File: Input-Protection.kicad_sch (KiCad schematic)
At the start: 0 parts

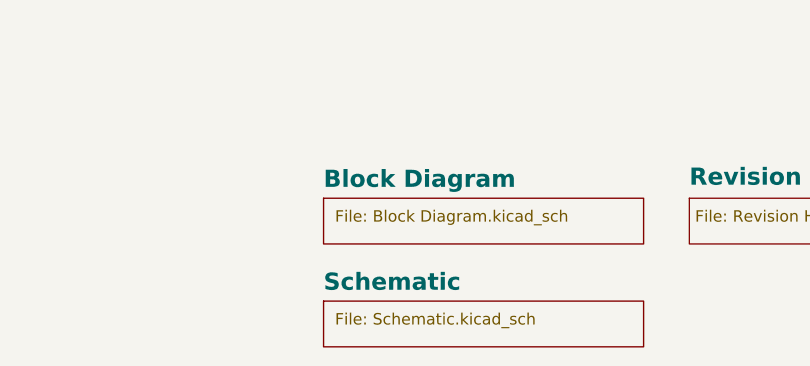
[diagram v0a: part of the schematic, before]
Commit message: fix: fix properties of actives with MPN
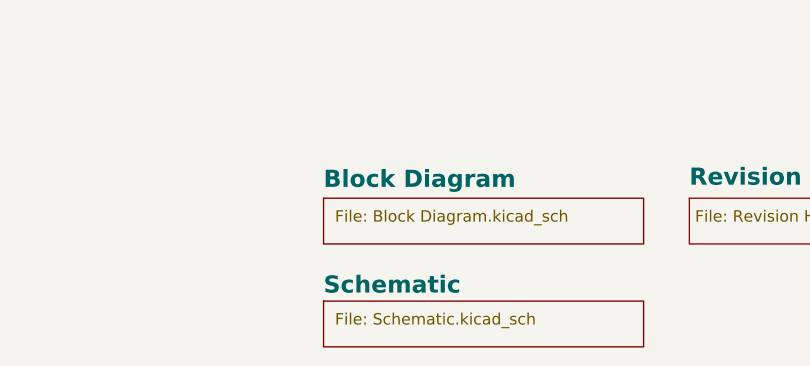
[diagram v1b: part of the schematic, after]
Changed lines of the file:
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@@
 		)
 		(property "Sheetname" "Schematic"
-			(at 299.72 312.6609 0)
+			(at 299.72 312.9784 0)
 			(effects
 				(font

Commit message: fix: template changes
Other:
- note added: "CHECKED - There shouldn't be any mistakes. Contact the engineer if found."
- note removed: "CHECKED - There shouldn't be any mistakes. Contact the engineer if you find any."
- note removed: "Date: ${RELEASE_DATE}"

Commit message: feat: preliminary pcb layout
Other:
- sheet Revision History renamed REVISION HISTORY
- removed sheet Block Diagram
- removed sheet Schematic
- added sheet ARCHITECTURE (Project Architecture.kicad_sch)
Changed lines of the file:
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@@
 	(text "TOP VIEW"
 		(exclude_from_sim no)
-		(at 22.86 166.37 0)
+		(at 27.94 166.37 0)
 		(effects
 			(font
@@
 		(effects
 			(font
-				(face "Arial")
 				(size 5 5)
 				(bold yes)
@@
 	(text_box "kibot_image_png_3d_viewer_angled_top"
 		(exclude_from_sim no)
-		(at 22.86 166.37 0)
+		(at 27.94 166.37 0)
 		(size 69.85 78.74)
 		(margins 1.905 1.905 1.905 1.905)
@@
 			(type dot)
 			(color 0 0 0 1)
+		)
+	)
+	(sheet
+		(at 299.72 313.69)
+		(size 35.56 5.08)
+		(exclude_from_sim no)
+		(in_bom yes)
+		(on_board yes)
+		(dnp no)
+		(stroke
+			(width 0.1524)
+			(type solid)
+		)
+		(fill
+			(color 0 0 0 0.0000)
+		)
+		(property "Sheetname" "ARCHITECTURE"
+			(at 299.72 312.9784 0)
+			(effects
+				(font
+					(face "Times New Roman")
+					(size 1.905 1.905)
+					(bold yes)
+					(color 0 0 0 1)
+				)
+				(justify left bottom)
+			)
+		)
+		(property "Sheetfile" "Project Architecture.kicad_sch"
+			(at 300.99 314.96 0)
+			(effects
+				(font
+					(face "Arial")
+					(size 1.27 1.27)
+				)
+				(justify left top)
+			)
+		)
+		(instances
+			(project "Input-Protection"
+				(path "/f9e05184-c88b-4a88-ae9c-ab2bdb32be7c"
+					(page "2")
+				)
+			)
 		)
 	)
@@
 			(color 0 0 0 0.0000)
 		)
-		(property "Sheetname" "Revision History"
+		(property "Sheetname" "REVISION HISTORY"
 			(at 340.36 300.99 0)
 			(effects
@@
 			(project "Input-Protection"
 				(path "/f9e05184-c88b-4a88-ae9c-ab2bdb32be7c"
-					(page "4")
+					(page "10")
 				)
 			)
-		)
-	)
-	(sheet
-		(at 299.72 302.26)
-		(size 35.56 5.08)
-		(exclude_from_sim no)
-		(in_bom yes)
-		(on_board yes)
-		(dnp no)
-		(stroke
-			(width 0.1524)
-			(type solid)
-		)
-		(fill
-			(color 0 0 0 0.0000)
-		)
-		(property "Sheetname" "Block Diagram"
-			(at 299.72 301.2309 0)
-			(effects
-				(font
-					(face "Times New Roman")
-					(size 1.905 1.905)
-					(bold yes)
-					(color 0 0 0 1)
-				)
-				(justify left bottom)
-			)
-		)
-		(property "Sheetfile" "Block Diagram.kicad_sch"
-			(at 300.99 303.53 0)
-			(effects
-				(font
-					(face "Arial")
-					(size 1.27 1.27)
-				)
-				(justify left top)
-			)
-		)
-		(instances
-			(project "Input-Protection"
-				(path "/f9e05184-c88b-4a88-ae9c-ab2bdb32be7c"
-					(page "2")
-				)
-			)
-		)
-	)
-	(sheet
-		(at 299.72 313.69)
-		(size 35.56 5.08)
-		(exclude_from_sim no)
-		(in_bom yes)
-		(on_board yes)
-		(dnp no)
-		(stroke
-			(width 0.1524)
-			(type solid)
-		)
-		(fill
-			(color 0 0 0 0.0000)
-		)
-		(property "Sheetname" "Schematic"
-			(at 299.72 312.9784 0)
-			(effects
-				(font
-					(face "Times New Roman")
-					(size 1.905 1.905)
-					(bold yes)
-					(color 0 0 0 1)
-				)
-				(justify left bottom)
-			)
-		)
-		(property "Sheetfile" "Schematic.kicad_sch"
-			(at 300.99 314.96 0)
-			(effects
-				(font
-					(face "Arial")
-					(size 1.27 1.27)
-				)
-				(justify left top)
-			)
-		)
-		(instances
-			(project "Input-Protection"
-				(path "/f9e05184-c88b-4a88-ae9c-ab2bdb32be7c"
-					(page "3")
-				)
-			)

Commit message: feat: revision B release
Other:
- note added: "CHECKED - PCB LAYOUT CHECKED, CONTACT ENGINEER IF MISTAKE FOUND"
- note added: "COMMENT"
- note added: "DRAFT - EARLY STAGE SCHEMATIC CAPTURE"
- note added: "INDEX"
- note added: "NOT FITTED COMPONENTS MARKED AS"
- note added: "PAGE"
- note added: "PRELIMINARY - LATE STAGE SCHEMATIC CAPTURE"
- note added: "RELEASED - READY FOR PRODUCTION"
- note added: "REV ${REVISION}"
- note added: "VARIANT: ${VARIANT}"
- note removed: "CHECKED - There shouldn't be any mistakes. Contact the engineer if found."
- note removed: "Comment"
- note removed: "DRAFT - Very early stage of schematic, ignore details."
- note removed: "Index"
- note removed: "Not fitted components are marked as"
- note removed: "PRELIMINARY - Close to final schematic."
- note removed: "Page"
- note removed: "RELEASED - A board with this schematic has been sent to production."
- note removed: "Rev ${REVISION}"
- note removed: "Variant: ${VARIANT}"
